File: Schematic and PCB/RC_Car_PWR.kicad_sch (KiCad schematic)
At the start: 3 parts, among them SW1 SW_Push, SW2 SW_Push, U1 ESP32-WROOM-32U

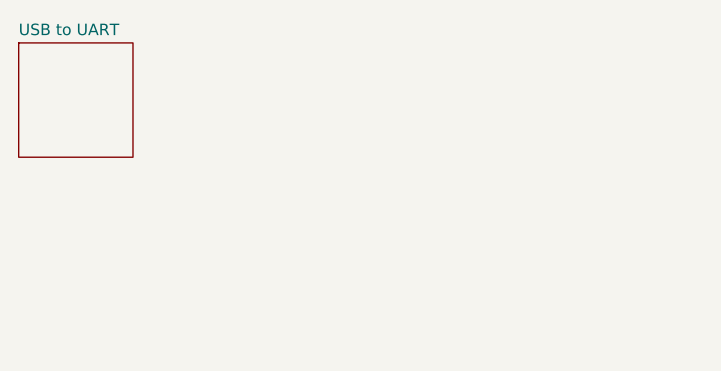
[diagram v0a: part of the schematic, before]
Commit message: Schematic update uart and power supply
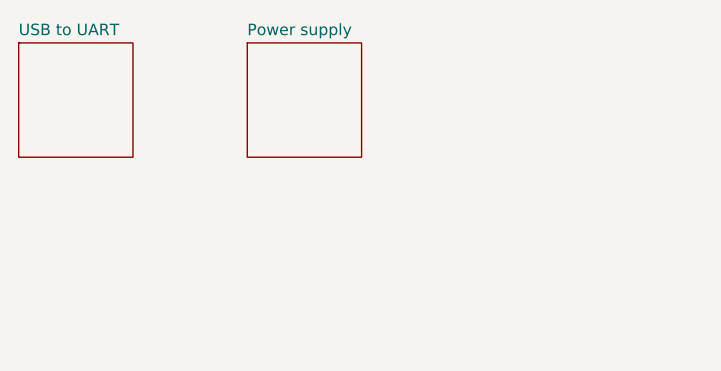
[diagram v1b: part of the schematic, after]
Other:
- added sheet Power supply (Power_supply.kicad_sch)
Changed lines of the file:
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@@
+		)
+	)
+	(sheet
+		(at 50.8 25.4)
+		(size 12.7 12.7)
+		(fields_autoplaced yes)
+		(stroke
+			(width 0.1524)
+			(type solid)
+		)
+		(fill
+			(color 0 0 0 0.0000)
+		)
+		(property "Sheetname" "Power supply"
+			(at 50.8 24.6884 0)
+			(effects
+				(font
+					(size 1.27 1.27)
+				)
+				(justify left bottom)
+			)
+		)
+		(property "Sheetfile" "Power_supply.kicad_sch"
+			(at 50.8 38.6846 0)
+			(effects
+				(font
+					(size 1.27 1.27)
+				)
+				(justify left top)
+				(hide yes)
+			)
+		)
+		(instances
+			(project "RC_Car_PWR"
+				(path "/97687706-6280-4d24-828f-729b51ecbb36"
+					(page "3")
+				)
+			)
 		)
 	)
